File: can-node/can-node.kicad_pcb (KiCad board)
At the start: 4 copper layers, 85 parts, among them J2 Conn_01x04_Pin, J3 USART1, Q1 DMP510DL-7, SW1 KMR2, U1 AP7375-33FDC, U2 STM32F105RBTx, U3 TCAN3404-Q1

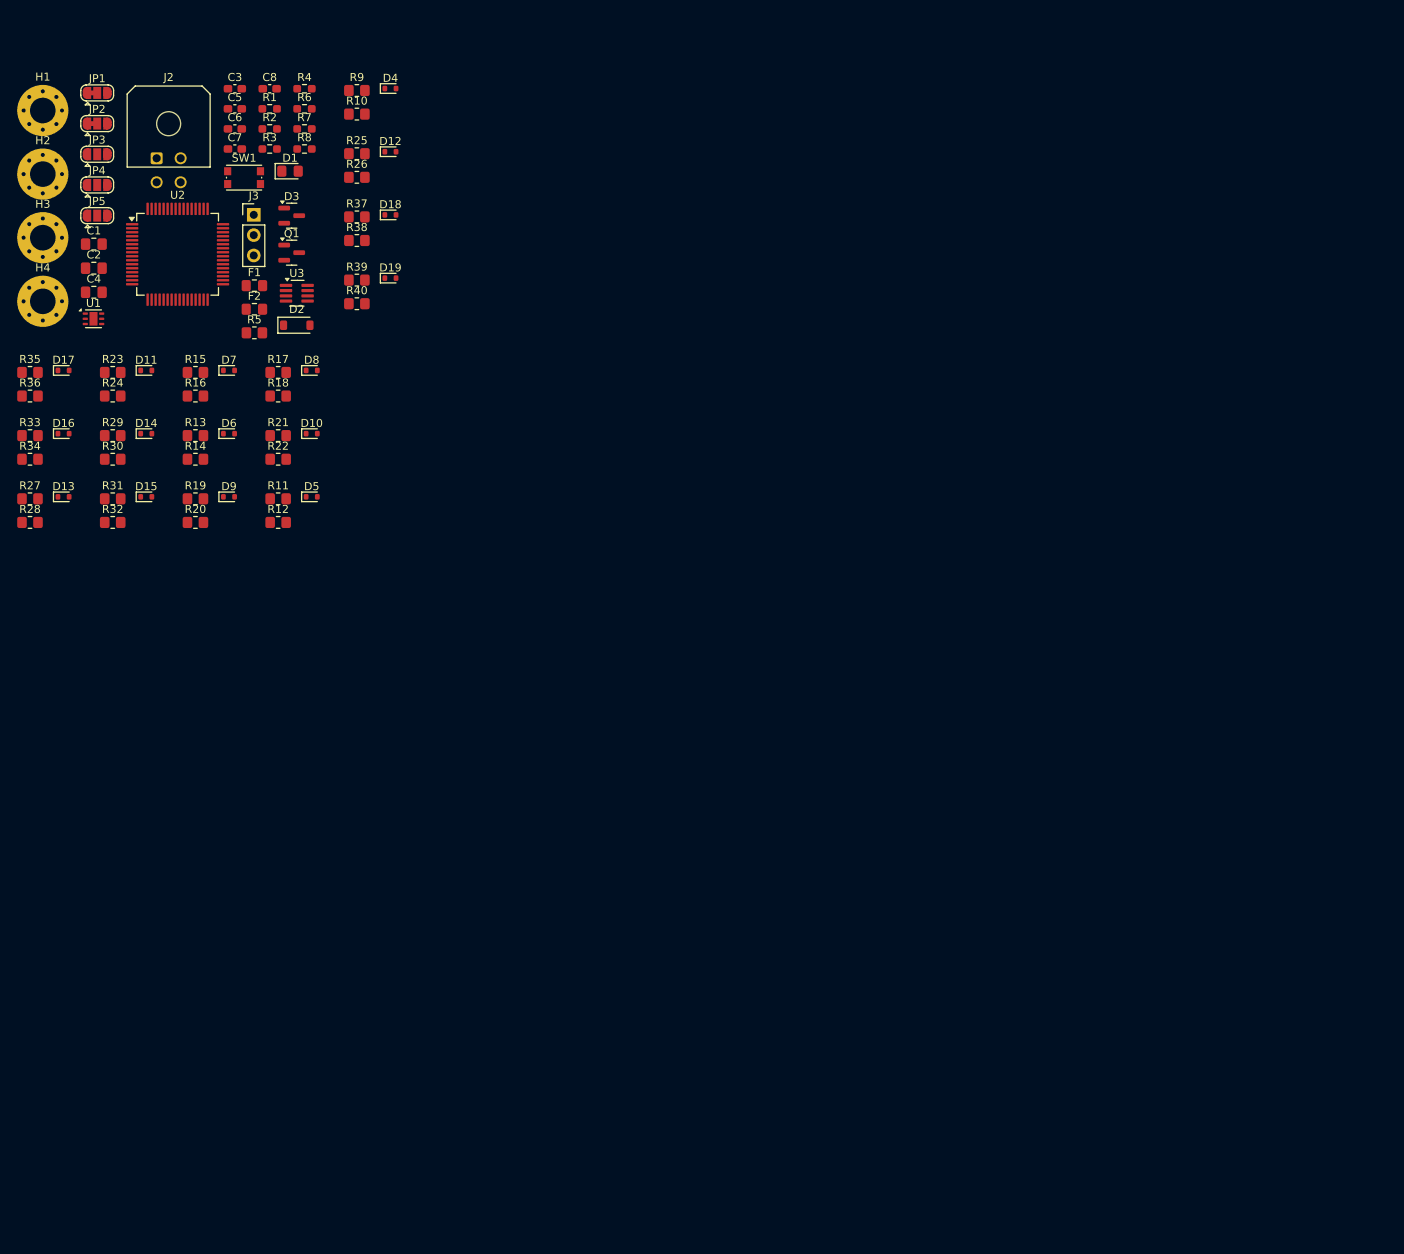
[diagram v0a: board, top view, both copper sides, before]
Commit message: finish routing (not silkscreen)
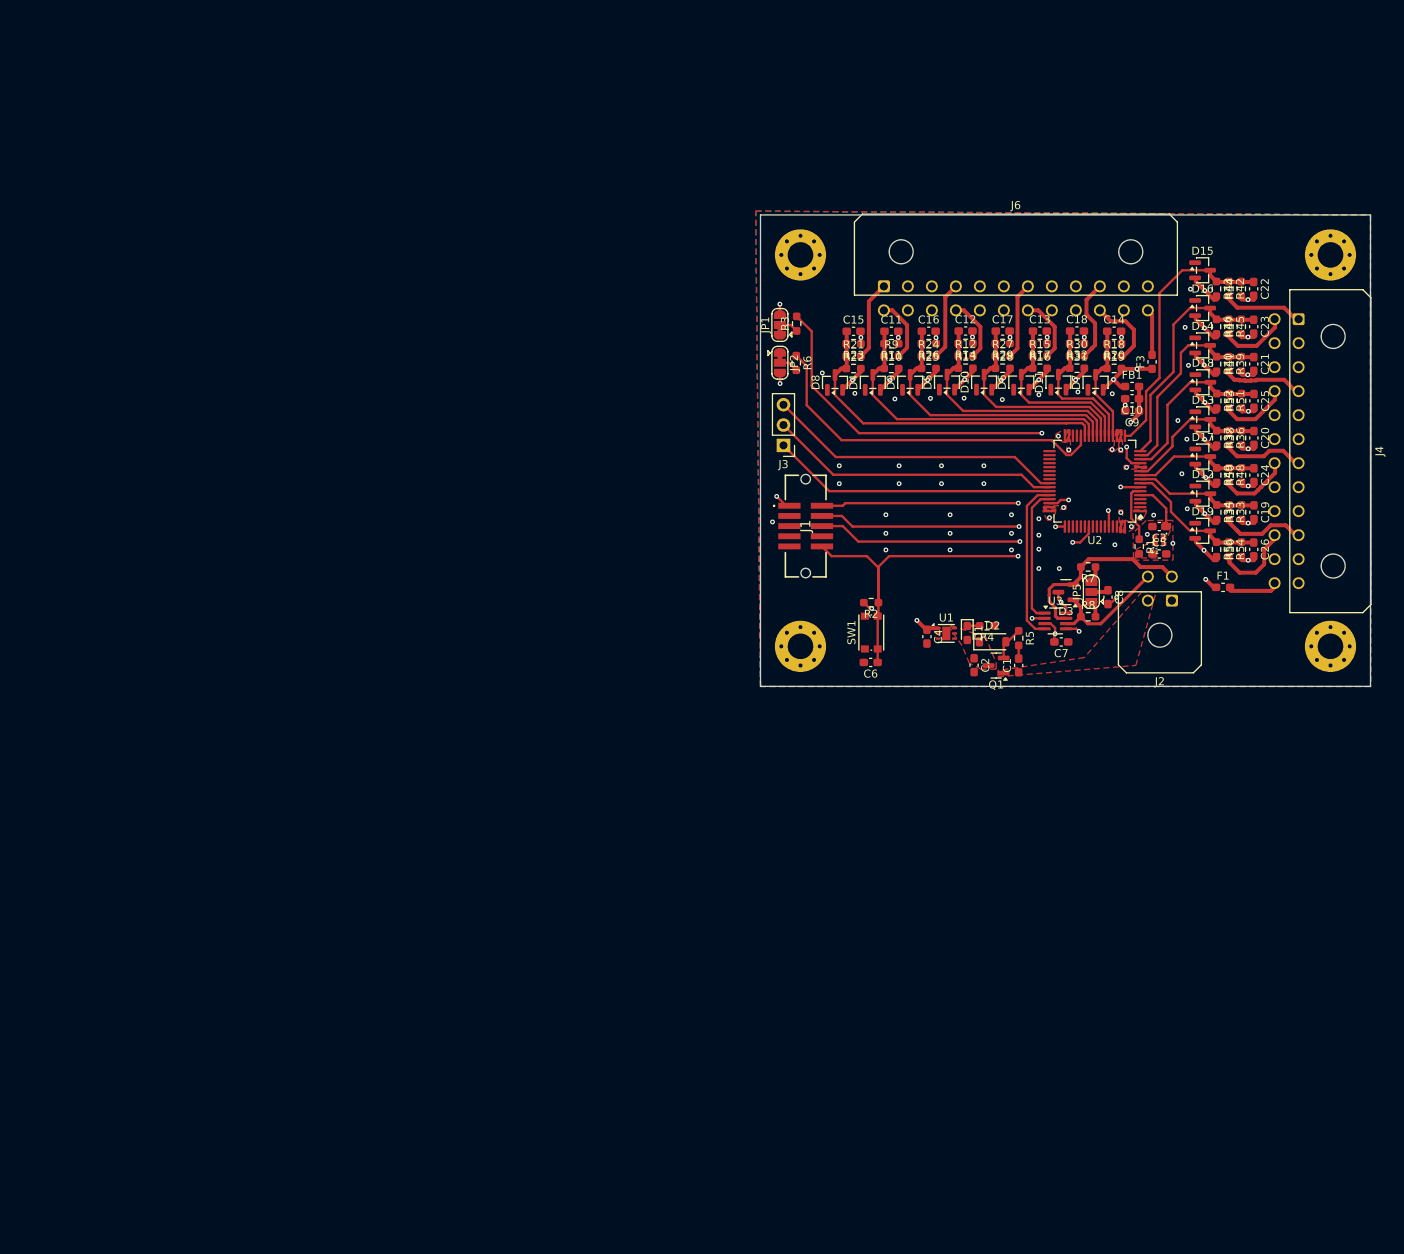
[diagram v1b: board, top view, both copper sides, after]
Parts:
- removed F2: 100mA, Fuse:Fuse_0805_2012Metric_Pad1.15x1.40mm_HandSolder
- removed JP3, JP4: SolderJumper_3_Open, Jumper:SolderJumper-3_P1.3mm_Open_RoundedPad1.0x1.5mm
- added C10: 10uF, Capacitor_SMD:C_0603_1608Metric_Pad1.08x0.95mm_HandSolder, F.Cu at (163.0, 63.8)
- added C11: 10nF, Capacitor_SMD:C_0603_1608Metric_Pad1.08x0.95mm_HandSolder, F.Cu at (132.9, 55.4)
- added C12: 10nF, Capacitor_SMD:C_0603_1608Metric_Pad1.08x0.95mm_HandSolder, F.Cu at (142.2, 55.3)
- added C13: 10nF, Capacitor_SMD:C_0603_1608Metric_Pad1.08x0.95mm_HandSolder, F.Cu at (151.5, 55.3)
- added C14: 10nF, Capacitor_SMD:C_0603_1608Metric_Pad1.08x0.95mm_HandSolder, F.Cu at (160.8, 55.4)
- added C15: 10nF, Capacitor_SMD:C_0603_1608Metric_Pad1.08x0.95mm_HandSolder, F.Cu at (128.2, 55.4)
- added C16: 10nF, Capacitor_SMD:C_0603_1608Metric_Pad1.08x0.95mm_HandSolder, F.Cu at (137.6, 55.4)
- added C17: 10nF, Capacitor_SMD:C_0603_1608Metric_Pad1.08x0.95mm_HandSolder, F.Cu at (146.8, 55.3)
- added C18: 10nF, Capacitor_SMD:C_0603_1608Metric_Pad1.08x0.95mm_HandSolder, F.Cu at (156.1, 55.3)
- added C19: 10nF, Capacitor_SMD:C_0603_1608Metric_Pad1.08x0.95mm_HandSolder, F.Cu at (178.2, 78.0)
- added C20: 10nF, Capacitor_SMD:C_0603_1608Metric_Pad1.08x0.95mm_HandSolder, F.Cu at (178.2, 68.7)
- added C21: 10nF, Capacitor_SMD:C_0603_1608Metric_Pad1.08x0.95mm_HandSolder, F.Cu at (178.2, 59.5)
- added C22: 10nF, Capacitor_SMD:C_0603_1608Metric_Pad1.08x0.95mm_HandSolder, F.Cu at (178.2, 50.1)
- added C23: 10nF, Capacitor_SMD:C_0603_1608Metric_Pad1.08x0.95mm_HandSolder, F.Cu at (178.2, 54.8)
- added C24: 10nF, Capacitor_SMD:C_0603_1608Metric_Pad1.08x0.95mm_HandSolder, F.Cu at (178.2, 73.3)
- added C25: 10nF, Capacitor_SMD:C_0603_1608Metric_Pad1.08x0.95mm_HandSolder, F.Cu at (178.2, 64.1)
- added C26: 10nF, Capacitor_SMD:C_0603_1608Metric_Pad1.08x0.95mm_HandSolder, F.Cu at (178.2, 82.6)
- added C9: 1uF, Capacitor_SMD:C_0603_1608Metric_Pad1.08x0.95mm_HandSolder, F.Cu at (163.0, 65.3)
- added F3: 100mA, Fuse:Fuse_0603_1608Metric_Pad1.05x0.95mm_HandSolder, F.Cu at (165.5, 59.2)
- added FB1: BLM18PG121SN1, Inductor_SMD:L_0603_1608Metric_Pad1.05x0.95mm_HandSolder, F.Cu at (163.0, 62.3)
- added J1: Conn_ARM_JTAG_SWD_10, SUFST:SHF10501LDSMLC, F.Cu at (122.2, 79.7)
- added J4: Molex MicroFit 3.0 24 pin (2x12) 43045-2401, Connector_Molex:Molex_Micro-Fit_3.0_43045-2400_2x12_P3.00mm_Horizontal, F.Cu at (183.8, 53.9)
- added J6: Molex MicroFit 3.0 24 pin (2x12) 43045-2401, Connector_Molex:Molex_Micro-Fit_3.0_43045-2400_2x12_P3.00mm_Horizontal, F.Cu at (132.0, 49.8)
- added R41: 10k, Resistor_SMD:R_0603_1608Metric_Pad0.98x0.95mm_HandSolder, F.Cu at (176.7, 59.5)
- added R42: 40k, Resistor_SMD:R_0603_1608Metric_Pad0.98x0.95mm_HandSolder, F.Cu at (175.1, 50.1)
- added R43: NC, Resistor_SMD:R_0603_1608Metric_Pad0.98x0.95mm_HandSolder, F.Cu at (173.5, 50.1)
- added R44: 10k, Resistor_SMD:R_0603_1608Metric_Pad0.98x0.95mm_HandSolder, F.Cu at (176.6, 50.1)
- added R45: 40k, Resistor_SMD:R_0603_1608Metric_Pad0.98x0.95mm_HandSolder, F.Cu at (175.1, 54.8)
- added R46: NC, Resistor_SMD:R_0603_1608Metric_Pad0.98x0.95mm_HandSolder, F.Cu at (173.6, 54.8)
- added R47: 10k, Resistor_SMD:R_0603_1608Metric_Pad0.98x0.95mm_HandSolder, F.Cu at (176.7, 54.8)
- added R48: 40k, Resistor_SMD:R_0603_1608Metric_Pad0.98x0.95mm_HandSolder, F.Cu at (175.1, 73.3)
- added R49: NC, Resistor_SMD:R_0603_1608Metric_Pad0.98x0.95mm_HandSolder, F.Cu at (173.6, 73.3)
- added R50: 10k, Resistor_SMD:R_0603_1608Metric_Pad0.98x0.95mm_HandSolder, F.Cu at (176.7, 73.3)
- added R51: 40k, Resistor_SMD:R_0603_1608Metric_Pad0.98x0.95mm_HandSolder, F.Cu at (175.1, 64.1)
- added R52: NC, Resistor_SMD:R_0603_1608Metric_Pad0.98x0.95mm_HandSolder, F.Cu at (173.6, 64.1)
- added R53: 10k, Resistor_SMD:R_0603_1608Metric_Pad0.98x0.95mm_HandSolder, F.Cu at (176.7, 64.1)
- added R54: 40k, Resistor_SMD:R_0603_1608Metric_Pad0.98x0.95mm_HandSolder, F.Cu at (175.1, 82.6)
- added R55: NC, Resistor_SMD:R_0603_1608Metric_Pad0.98x0.95mm_HandSolder, F.Cu at (173.6, 82.6)
- added R56: 10k, Resistor_SMD:R_0603_1608Metric_Pad0.98x0.95mm_HandSolder, F.Cu at (176.7, 82.6)
- added Y1: ECS-250-10-47Q-CES-TR, SUFST:Resonator_SMD_ECS_ECX-1247Q_1.6x1.2x0.3mm, F.Cu at (166.4, 81.5)
- C1, C2, C4: footprint Capacitor_SMD:C_0805_2012Metric_Pad1.18x1.45mm_HandSolder -> Capacitor_SMD:C_0603_1608Metric_Pad1.08x0.95mm_HandSolder
- D1: footprint LED_SMD:LED_0805_2012Metric_Pad1.15x1.40mm_HandSolder -> LED_SMD:LED_0603_1608Metric_Pad1.05x0.95mm_HandSolder
- D10, D11, D12, D13, D14, D15, D16, D17, D18, D19, D4, D5, D6, D7, D8, D9: value BZT585B3V3T-7 -> BAT54S; footprint Diode_SMD:D_SOD-523 -> Package_TO_SOT_SMD:SOT-23
- F1: footprint Fuse:Fuse_0805_2012Metric_Pad1.15x1.40mm_HandSolder -> Fuse:Fuse_0603_1608Metric_Pad1.05x0.95mm_HandSolder
- R10, R16, R22, R28, R34, R40: value 40k -> NC; footprint Resistor_SMD:R_0805_2012Metric_Pad1.20x1.40mm_HandSolder -> Resistor_SMD:R_0603_1608Metric_Pad0.98x0.95mm_HandSolder
- R11, R12, R17, R18, R23, R24, R29, R30, R35, R36, R5: footprint Resistor_SMD:R_0805_2012Metric_Pad1.20x1.40mm_HandSolder -> Resistor_SMD:R_0603_1608Metric_Pad0.98x0.95mm_HandSolder
- R13, R19, R25, R31, R37: value 10k -> NC; footprint Resistor_SMD:R_0805_2012Metric_Pad1.20x1.40mm_HandSolder -> Resistor_SMD:R_0603_1608Metric_Pad0.98x0.95mm_HandSolder
- R14, R20, R26, R32, R38: value 40k -> 10k; footprint Resistor_SMD:R_0805_2012Metric_Pad1.20x1.40mm_HandSolder -> Resistor_SMD:R_0603_1608Metric_Pad0.98x0.95mm_HandSolder
- R15, R21, R27, R33, R39, R9: value 10k -> 40k; footprint Resistor_SMD:R_0805_2012Metric_Pad1.20x1.40mm_HandSolder -> Resistor_SMD:R_0603_1608Metric_Pad0.98x0.95mm_HandSolder
- moved H4 166.6 mm to (187.8, 94.8)
- moved H2 161.3 mm to (187.8, 45.8)
- moved R35 152.4 mm to (176.7, 78.0), turned to 90 degrees
- moved R33 150.2 mm to (175.1, 78.0), turned to -90 degrees
- moved R36 150.0 mm to (175.1, 68.7), turned to -90 degrees
- moved R34 148.5 mm to (173.6, 78.0), turned to -90 degrees
- moved D16 143.2 mm to (171.8, 52.5)
- moved D17 142.8 mm to (171.8, 71.0)
- moved D13 142.7 mm to (171.8, 66.4)
- moved J2 138.4 mm to (168.0, 89.0), turned to 180 degrees
- moved D15 135.0 mm to (171.8, 47.7)
- moved JP5 132.9 mm to (157.9, 88.0), turned to 90 degrees
- moved D14 132.5 mm to (171.8, 57.1)
- moved C5 128.3 mm to (166.4, 83.2)
- moved C3 127.9 mm to (166.4, 79.8), turned to 180 degrees
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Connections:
- C4 pad 1: +3.3V -> +3V3
- C7 pad 2: +3.3V -> +3V3
- D10 pad 1: /ADC_1_2 -> GND
- D10 pad 2: GND -> +3V3
- D11 pad 1: /ADC_1_1 -> GND
- D11 pad 2: GND -> +3V3
- D12 pad 1: /ADC_1_0 -> GND
- D12 pad 2: GND -> +3V3
- D13 pad 1: /ADC_0_7 -> GND
- D13 pad 2: GND -> +3V3
- D14 pad 1: /ADC_0_6 -> GND
- D14 pad 2: GND -> +3V3
- D15 pad 1: /ADC_0_5 -> GND
- D15 pad 2: GND -> +3V3
- D16 pad 1: /ADC_0_4 -> GND
- D16 pad 2: GND -> +3V3
- D17 pad 1: /ADC_0_1 -> GND
- D17 pad 2: GND -> +3V3
- D18 pad 1: /ADC_0_3 -> GND
- D18 pad 2: GND -> +3V3
- D19 pad 1: /ADC_0_2 -> GND
- D19 pad 2: GND -> +3V3
- D4 pad 1: /ADC_1_7 -> GND
- D4 pad 2: GND -> +3V3
- D5 pad 1: /ADC_0_0 -> GND
- D5 pad 2: GND -> +3V3
- D6 pad 1: /ADC_1_6 -> GND
- D6 pad 2: GND -> +3V3
- D7 pad 1: /ADC_1_5 -> GND
- D7 pad 2: GND -> +3V3
- D8 pad 1: /ADC_1_4 -> GND
- D8 pad 2: GND -> +3V3
- D9 pad 1: /ADC_1_3 -> GND
- D9 pad 2: GND -> +3V3
- F1 pad 1: GND -> +3V3
- F1 pad 2: Net-(JP3-A) -> /Generic ADC Input Group1/3V3_FUSED
- JP1 pad 3: +3.3V -> +3V3
- R10 pad 1: /ADC_1_7 -> /ADC_0_4
- R10 pad 2: /ClampedDivider15/IN -> +3V3
- R11 pad 2: /ADC_0_0 -> /ADC_0_4
- R12 pad 1: /ADC_0_0 -> /ADC_0_5
- R12 pad 2: /ClampedDivider16/IN -> /Generic ADC Input Group/ClampedDivider17/IN
- R13 pad 1: GND -> /ADC_0_5
- R13 pad 2: /ADC_1_6 -> +3V3
- R14 pad 1: /ADC_1_6 -> GND
- R14 pad 2: /ClampedDivider17/IN -> /ADC_0_5
- R15 pad 1: GND -> /ADC_0_6
- R15 pad 2: /ADC_1_5 -> /Generic ADC Input Group/ClampedDivider18/IN
- R16 pad 1: /ADC_1_5 -> /ADC_0_6
- R16 pad 2: /ClampedDivider18/IN -> +3V3
- R17 pad 2: /ADC_1_4 -> /ADC_0_6
- R18 pad 1: /ADC_1_4 -> /ADC_0_7
- R18 pad 2: /ClampedDivider19/IN -> /Generic ADC Input Group/ClampedDivider19/IN
- R19 pad 1: GND -> /ADC_0_7
- R19 pad 2: /ADC_1_3 -> +3V3
- R20 pad 1: /ADC_1_3 -> GND
- R20 pad 2: /ClampedDivider20/IN -> /ADC_0_7
- R21 pad 1: GND -> /ADC_0_0
- R21 pad 2: /ADC_1_2 -> /Generic ADC Input Group/ClampedDivider20/IN
- R22 pad 1: /ADC_1_2 -> /ADC_0_0
- R22 pad 2: /ClampedDivider21/IN -> +3V3
- R23 pad 2: /ADC_1_1 -> /ADC_0_0
- R24 pad 1: /ADC_1_1 -> /ADC_0_1
- R24 pad 2: /ClampedDivider22/IN -> /Generic ADC Input Group/ClampedDivider21/IN
- R25 pad 1: GND -> /ADC_0_1
- R25 pad 2: /ADC_1_0 -> +3V3
- R26 pad 1: /ADC_1_0 -> GND
- R26 pad 2: /ClampedDivider23/IN -> /ADC_0_1
- R27 pad 1: GND -> /ADC_0_2
- R27 pad 2: /ADC_0_7 -> /Generic ADC Input Group/ClampedDivider22/IN
- R28 pad 1: /ADC_0_7 -> /ADC_0_2
- R28 pad 2: /ClampedDivider24/IN -> +3V3
- R29 pad 2: /ADC_0_6 -> /ADC_0_2
- R30 pad 1: /ADC_0_6 -> /ADC_0_3
- R30 pad 2: /ClampedDivider25/IN -> /Generic ADC Input Group/ClampedDivider23/IN
- R31 pad 1: GND -> /ADC_0_3
- R31 pad 2: /ADC_0_5 -> +3V3
- R32 pad 1: /ADC_0_5 -> GND
- R32 pad 2: /ClampedDivider26/IN -> /ADC_0_3
- R33 pad 1: GND -> /ADC_1_3
- R33 pad 2: /ADC_0_4 -> /Generic ADC Input Group1/ClampedDivider23/IN
- R34 pad 1: /ADC_0_4 -> /ADC_1_3
- R34 pad 2: /ClampedDivider27/IN -> +3V3
- R35 pad 2: /ADC_0_1 -> /ADC_1_3
- R36 pad 1: /ADC_0_1 -> /ADC_1_2
- R36 pad 2: /ClampedDivider28/IN -> /Generic ADC Input Group1/ClampedDivider22/IN
- R37 pad 1: GND -> /ADC_1_2
- R37 pad 2: /ADC_0_3 -> +3V3
- R38 pad 1: /ADC_0_3 -> GND
- R38 pad 2: /ClampedDivider29/IN -> /ADC_1_2
- R39 pad 1: GND -> /ADC_1_1
- R39 pad 2: /ADC_0_2 -> /Generic ADC Input Group1/ClampedDivider21/IN
- R40 pad 1: /ADC_0_2 -> /ADC_1_1
- R40 pad 2: /ClampedDivider30/IN -> +3V3
- R9 pad 1: GND -> /ADC_0_4
- R9 pad 2: /ADC_1_7 -> /Generic ADC Input Group/ClampedDivider16/IN
- U1 pad 1: +3.3V -> +3V3
- U2 pad 1: +3.3V -> +3V3
- U2 pad 10: /ADC_0_2 -> /ADC_1_6
- U2 pad 11: /ADC_0_3 -> /ADC_1_2
- U2 pad 13: +3.3V -> +3V3A
- U2 pad 14: /ADC_0_4 -> /ADC_1_5
- U2 pad 15: /ADC_0_5 -> /ADC_1_1
- U2 pad 16: /ADC_0_6 -> /ADC_1_4
- U2 pad 17: /ADC_0_7 -> /ADC_1_0
- U2 pad 19: +3.3V -> +3V3
- U2 pad 20: /ADC_1_7 -> /ADC_0_7
- U2 pad 21: /ADC_1_6 -> /ADC_0_3
- U2 pad 22: /ADC_1_5 -> /ADC_0_6
- U2 pad 23: /ADC_1_4 -> /ADC_0_2
- U2 pad 24: /ADC_1_3 -> /ADC_0_5
- U2 pad 25: /ADC_1_2 -> /ADC_0_1
- U2 pad 26: /ADC_1_1 -> /ADC_0_4
- U2 pad 27: /ADC_1_0 -> /ADC_0_0
- U2 pad 32: +3.3V -> +3V3
- U2 pad 48: +3.3V -> +3V3
- U2 pad 64: +3.3V -> +3V3
- U2 pad 8: /ADC_0_0 -> /ADC_1_7
- U2 pad 9: /ADC_0_1 -> /ADC_1_3
- U3 pad 3: +3.3V -> +3V3
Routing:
- net +3V3: track 0.00 -> 77.9 mm, vias 0 -> 29
- net /NReset: track 0.00 -> 63.1 mm, vias 0 -> 2
- net Net-(U2-BOOT0): track 0.00 -> 55.8 mm, vias 0 -> 2
- net Net-(U2-PB2): track 0.00 -> 45.3 mm
- net GND: track 0.00 -> 43.4 mm, vias 0 -> 69
- net /ADC_0_0: track 0.00 -> 43.0 mm
- net /ADC_0_4: track 0.00 -> 38.9 mm
- net USART1_CK: track 0.00 -> 37.3 mm
- net USART1_TX: track 0.00 -> 36.5 mm
- net USART1_RX: track 0.00 -> 35.6 mm
- net SYS_JTDO: track 0.00 -> 35.5 mm, vias 0 -> 2
- net /ADC_0_1: track 0.00 -> 34.9 mm
- net /ADC_1_0: track 0.00 -> 33.9 mm
- net SYS_JTMS-SWDIO: track 0.00 -> 33.7 mm, vias 0 -> 2
- net SYS_JTCK-SW: track 0.00 -> 31.0 mm, vias 0 -> 2
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- added copper zone on F.Cu, net +3V3
- added copper zone on In2.Cu, net +3V3
- added copper zone on F.Cu, net +GLV
- added copper zone on F.Cu, net +GLV_PROT
- added copper zone on In1.Cu, net /Generic ADC Input Group/3V3_FUSED
- added copper zone on In1.Cu, net /Generic ADC Input Group1/3V3_FUSED
- added copper zone on B.Cu, net GND
- added copper zone on F.Cu, net GND
- added copper zone on F.Cu, net Net-(C5-Pad1)
- added copper zone on F.Cu, net Net-(U2-PD0)
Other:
- board outline added: 76.3 x 58.9 mm

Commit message: switch B.Cu and In1.Cu routing, update silkscreen and other fixes
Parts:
- added G***: LOGO, SUFST:SUFST, F.Cu at (139.7, 76.1)
- moved R1 9.44 mm to (168.1, 73.8), turned to 0 degrees
- moved C5 7.18 mm to (169.2, 76.6), turned to -90 degrees
- moved Y1 5.30 mm to (166.6, 76.2), turned to 0 degrees
- moved C3 1.94 mm to (166.8, 77.9), turned to 0 degrees
- moved U1 1.52 mm to (139.8, 94.7)
- moved C4 1.52 mm to (137.4, 95.0)
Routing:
- net Net-(U2-BOOT0): track 55.8 -> 63.9 mm
- net /ADC_1_7: track 18.3 -> 24.3 mm
- net Net-(C5-Pad1): track 0.00 -> 4.59 mm
- net GND: track 43.4 -> 47.0 mm, vias 69 -> 98
- net Net-(U2-PD1): track 7.40 -> 4.09 mm
- net Net-(U2-PD0): track 6.18 -> 3.47 mm
- net SYS_JTCK-SW: track 31.0 -> 29.9 mm
- net /ADC_1_3: track 15.9 -> 16.8 mm
- net +3V3: track 77.9 -> 77.1 mm, vias 29 -> 38
- net Net-(D2-A+): track 4.30 -> 3.68 mm
- added copper zone on B.Cu, net /Generic ADC Input Group/3V3_FUSED
- added copper zone on B.Cu, net /Generic ADC Input Group1/3V3_FUSED
- added copper zone on In1.Cu, net GND
- added copper zone on In2.Cu, net GND
- removed copper zone on In1.Cu, net /Generic ADC Input Group/3V3_FUSED
- removed copper zone on In1.Cu, net /Generic ADC Input Group1/3V3_FUSED
- removed copper zone on F.Cu, net Net-(C5-Pad1)
- removed copper zone on F.Cu, net Net-(U2-PD0)
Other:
- outline, holes or cut-outs redrawn
- board text added: "${REFERENCE}"
- board text added: "0"
- board text added: "1"
- board text added: "Author: Antmicro"
- board text added: "BAT54S"
- board text added: "BOOT"
- board text added: "CAP"
- board text added: "CK"
- board text added: "DOWN"
- board text added: "Designed by Sam and Martin"
- board text added: "HUB"
- board text added: "JTAG"
- board text added: "License: Apache-2.0"
- board text added: "Molex MicroFit 3.0 24 pin (2x12) 43045-2401"
- board text added: "Molex Microfit 3.0 4-pin (2x2) 43045-0400"
- board text added: "RX"
- board text added: "SERIES"
- board text added: "Sensor"
- board text added: "TX"
- board text added: "UART"
- board text added: "UP"
- board text added: "v1.0"

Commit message: forgot to save
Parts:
- added U10: TLV9101IDBVR, Package_TO_SOT_SMD:SOT-23-5_HandSoldering, F.Cu at (89.6, 26.7)
- added U11: TLV9101IDBVR, Package_TO_SOT_SMD:SOT-23-5_HandSoldering, F.Cu at (105.2, 19.9)
- added U12: TLV9101IDBVR, Package_TO_SOT_SMD:SOT-23-5_HandSoldering, F.Cu at (105.2, 26.7)
- added U13: TLV9101IDBVR, Package_TO_SOT_SMD:SOT-23-5_HandSoldering, F.Cu at (97.4, 33.4)
- added U14: TLV9101IDBVR, Package_TO_SOT_SMD:SOT-23-5_HandSoldering, F.Cu at (105.2, 40.2)
- added U15: TLV9101IDBVR, Package_TO_SOT_SMD:SOT-23-5_HandSoldering, F.Cu at (105.2, 33.4)
- added U16: TLV9101IDBVR, Package_TO_SOT_SMD:SOT-23-5_HandSoldering, F.Cu at (81.8, 26.7)
- added U17: TLV9101IDBVR, Package_TO_SOT_SMD:SOT-23-5_HandSoldering, F.Cu at (81.8, 33.4)
- added U18: TLV9101IDBVR, Package_TO_SOT_SMD:SOT-23-5_HandSoldering, F.Cu at (81.8, 19.9)
- added U19: TLV9101IDBVR, Package_TO_SOT_SMD:SOT-23-5_HandSoldering, F.Cu at (97.4, 19.9)
- added U4: TLV9101IDBVR, Package_TO_SOT_SMD:SOT-23-5_HandSoldering, F.Cu at (89.6, 40.2)
- added U5: TLV9101IDBVR, Package_TO_SOT_SMD:SOT-23-5_HandSoldering, F.Cu at (89.6, 33.4)
- added U6: TLV9101IDBVR, Package_TO_SOT_SMD:SOT-23-5_HandSoldering, F.Cu at (97.4, 26.7)
- added U7: TLV9101IDBVR, Package_TO_SOT_SMD:SOT-23-5_HandSoldering, F.Cu at (97.4, 40.2)
- added U8: TLV9101IDBVR, Package_TO_SOT_SMD:SOT-23-5_HandSoldering, F.Cu at (81.8, 40.2)
- added U9: TLV9101IDBVR, Package_TO_SOT_SMD:SOT-23-5_HandSoldering, F.Cu at (89.6, 19.9)
- J4: value Molex MicroFit 3.0 24 pin (2x12) 43045-2401 -> Harwin M80-5402642; footprint Connector_Molex:Molex_Micro-Fit_3.0_43045-2400_2x12_P3.00mm_Horizontal -> SUFST:M80-5402642
- J5: renamed from J6; value Molex MicroFit 3.0 24 pin (2x12) 43045-2401 -> Harwin M80-5402642; footprint Connector_Molex:Molex_Micro-Fit_3.0_43045-2400_2x12_P3.00mm_Horizontal -> SUFST:M80-5402642
- moved C19 98.6 mm to (79.7, 75.9), turned to 0 degrees
- moved R35 97.2 mm to (79.7, 83.5), turned to 0 degrees
- moved R33 95.5 mm to (79.7, 78.5), turned to 0 degrees
- moved R34 93.9 mm to (79.7, 81.0), turned to 0 degrees
- moved R41 89.0 mm to (90.9, 83.5), turned to 0 degrees
- moved C21 88.8 mm to (90.9, 75.9), turned to 0 degrees
- moved D12 87.5 mm to (84.3, 77.1)
- moved C20 87.4 mm to (90.9, 63.9), turned to 0 degrees
- moved R39 86.3 mm to (90.9, 78.5), turned to 0 degrees
- moved R38 85.8 mm to (90.9, 71.4), turned to 0 degrees
- moved R40 85.4 mm to (90.9, 81.0), turned to 0 degrees
- moved R36 84.2 mm to (90.9, 66.4), turned to 0 degrees
- moved R37 82.6 mm to (90.9, 68.9), turned to 0 degrees
- moved R44 77.4 mm to (102.2, 71.4), turned to 0 degrees
- moved C22 77.2 mm to (102.2, 63.9), turned to 0 degrees
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- renumbered C3 to C1, C4 to C10, C5 to C2, C6 to C3, C7 to C4, C8 to C5, C9 to C6, C10 to C7, C1 to C8, C2 to C9, D3 to D1, D1 to D3, F3 to F2, JP5 to JP2, JP2 to JP3, R7 to R4, R8 to R5, R5 to R7, R4 to R8, U3 to U1, U1 to U3
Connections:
- C15 pad 1: /ADC_0_0 -> /ADC_1_3
- C16 pad 1: /ADC_0_1 -> /ADC_1_2
- C17 pad 1: /ADC_0_2 -> /ADC_1_1
- C18 pad 1: /ADC_0_3 -> /ADC_1_0
- C19 pad 1: /ADC_1_3 -> /ADC_0_0
- C20 pad 1: /ADC_1_2 -> /ADC_0_1
- C21 pad 1: /ADC_1_1 -> /ADC_0_2
- C22 pad 1: /ADC_1_0 -> /ADC_0_3
- D10 pad 3: /ADC_0_2 -> /ADC_1_1
- D11 pad 3: /ADC_0_3 -> /ADC_1_0
- D12 pad 3: /ADC_1_3 -> /ADC_0_0
- D13 pad 3: /ADC_1_2 -> /ADC_0_1
- D14 pad 3: /ADC_1_1 -> /ADC_0_2
- D15 pad 3: /ADC_1_0 -> /ADC_0_3
- D8 pad 3: /ADC_0_0 -> /ADC_1_3
- D9 pad 3: /ADC_0_1 -> /ADC_1_2
- J4 pad 1: /Generic ADC Input Group1/ClampedDivider20/IN -> unconnected-(J4-Pin_1-Pad1)
- J4 pad 10: /Generic ADC Input Group1/ClampedDivider23/IN -> /Generic ADC Input Group1/3V3_FUSED
- J4 pad 11: GND -> /Generic ADC Input Group1/ClampedDivider23/IN
- J4 pad 12: /Generic ADC Input Group1/3V3_FUSED -> GND
- J4 pad 13: /Generic ADC Input Group1/ClampedDivider16/IN -> /Generic ADC Input Group1/3V3_FUSED
- J4 pad 14: GND -> unconnected-(J4-Pin_14-Pad14)
- J4 pad 15: /Generic ADC Input Group1/3V3_FUSED -> /Generic ADC Input Group1/ClampedDivider16/IN
- J4 pad 16: /Generic ADC Input Group1/ClampedDivider17/IN -> GND
- J4 pad 17: GND -> /Generic ADC Input Group1/3V3_FUSED
- J4 pad 18: /Generic ADC Input Group1/3V3_FUSED -> /Generic ADC Input Group1/ClampedDivider17/IN
- J4 pad 19: /Generic ADC Input Group1/ClampedDivider18/IN -> GND
- J4 pad 2: GND -> /Generic ADC Input Group1/ClampedDivider20/IN
- J4 pad 20: GND -> /Generic ADC Input Group1/3V3_FUSED
- J4 pad 21: /Generic ADC Input Group1/3V3_FUSED -> /Generic ADC Input Group1/ClampedDivider18/IN
- J4 pad 22: /Generic ADC Input Group1/ClampedDivider19/IN -> GND
- J4 pad 23: GND -> /Generic ADC Input Group1/3V3_FUSED
- J4 pad 24: /Generic ADC Input Group1/3V3_FUSED -> /Generic ADC Input Group1/ClampedDivider19/IN
- J4 pad 3: /Generic ADC Input Group1/3V3_FUSED -> GND
- J4 pad 4: /Generic ADC Input Group1/ClampedDivider21/IN -> /Generic ADC Input Group1/3V3_FUSED
- J4 pad 5: GND -> /Generic ADC Input Group1/ClampedDivider21/IN
- J4 pad 6: /Generic ADC Input Group1/3V3_FUSED -> GND
- J4 pad 7: /Generic ADC Input Group1/ClampedDivider22/IN -> /Generic ADC Input Group1/3V3_FUSED
- J4 pad 8: GND -> /Generic ADC Input Group1/ClampedDivider22/IN
- J4 pad 9: /Generic ADC Input Group1/3V3_FUSED -> GND
- J5 pad 1: /Generic ADC Input Group/ClampedDivider20/IN -> unconnected-(J5-Pin_1-Pad1)
- J5 pad 10: /Generic ADC Input Group/ClampedDivider23/IN -> /Generic ADC Input Group/3V3_FUSED
- J5 pad 11: GND -> /Generic ADC Input Group/ClampedDivider23/IN
- J5 pad 12: /Generic ADC Input Group/3V3_FUSED -> GND
- J5 pad 13: /Generic ADC Input Group/ClampedDivider16/IN -> /Generic ADC Input Group/3V3_FUSED
- J5 pad 14: GND -> unconnected-(J5-Pin_14-Pad14)
- J5 pad 15: /Generic ADC Input Group/3V3_FUSED -> /Generic ADC Input Group/ClampedDivider16/IN
- J5 pad 16: /Generic ADC Input Group/ClampedDivider17/IN -> GND
- J5 pad 17: GND -> /Generic ADC Input Group/3V3_FUSED
- J5 pad 18: /Generic ADC Input Group/3V3_FUSED -> /Generic ADC Input Group/ClampedDivider17/IN
- J5 pad 19: /Generic ADC Input Group/ClampedDivider18/IN -> GND
- J5 pad 2: GND -> /Generic ADC Input Group/ClampedDivider20/IN
- J5 pad 20: GND -> /Generic ADC Input Group/3V3_FUSED
- J5 pad 21: /Generic ADC Input Group/3V3_FUSED -> /Generic ADC Input Group/ClampedDivider18/IN
- J5 pad 22: /Generic ADC Input Group/ClampedDivider19/IN -> GND
- J5 pad 23: GND -> /Generic ADC Input Group/3V3_FUSED
- J5 pad 24: /Generic ADC Input Group/3V3_FUSED -> /Generic ADC Input Group/ClampedDivider19/IN
- J5 pad 3: /Generic ADC Input Group/3V3_FUSED -> GND
- J5 pad 4: /Generic ADC Input Group/ClampedDivider21/IN -> /Generic ADC Input Group/3V3_FUSED
- J5 pad 5: GND -> /Generic ADC Input Group/ClampedDivider21/IN
- J5 pad 6: /Generic ADC Input Group/3V3_FUSED -> GND
- J5 pad 7: /Generic ADC Input Group/ClampedDivider22/IN -> /Generic ADC Input Group/3V3_FUSED
- J5 pad 8: GND -> /Generic ADC Input Group/ClampedDivider22/IN
- J5 pad 9: /Generic ADC Input Group/3V3_FUSED -> GND
- R12 pad 2: /Generic ADC Input Group/ClampedDivider17/IN -> Net-(U5--)
- R15 pad 2: /Generic ADC Input Group/ClampedDivider18/IN -> Net-(U6--)
- R18 pad 2: /Generic ADC Input Group/ClampedDivider19/IN -> Net-(U7--)
- R21 pad 1: /ADC_0_0 -> /ADC_1_3
- R21 pad 2: /Generic ADC Input Group/ClampedDivider20/IN -> Net-(U11--)
- R22 pad 1: /ADC_0_0 -> /ADC_1_3
- R23 pad 2: /ADC_0_0 -> /ADC_1_3
- R24 pad 1: /ADC_0_1 -> /ADC_1_2
- R24 pad 2: /Generic ADC Input Group/ClampedDivider21/IN -> Net-(U10--)
- R25 pad 1: /ADC_0_1 -> /ADC_1_2
- R26 pad 2: /ADC_0_1 -> /ADC_1_2
- R27 pad 1: /ADC_0_2 -> /ADC_1_1
- R27 pad 2: /Generic ADC Input Group/ClampedDivider22/IN -> Net-(U9--)
- R28 pad 1: /ADC_0_2 -> /ADC_1_1
- R29 pad 2: /ADC_0_2 -> /ADC_1_1
- R30 pad 1: /ADC_0_3 -> /ADC_1_0
- R30 pad 2: /Generic ADC Input Group/ClampedDivider23/IN -> Net-(U8--)
- R31 pad 1: /ADC_0_3 -> /ADC_1_0
- R32 pad 2: /ADC_0_3 -> /ADC_1_0
- R33 pad 1: /ADC_1_3 -> /ADC_0_0
- R33 pad 2: /Generic ADC Input Group1/ClampedDivider23/IN -> Net-(U12--)
- R34 pad 1: /ADC_1_3 -> /ADC_0_0
- R35 pad 2: /ADC_1_3 -> /ADC_0_0
- R36 pad 1: /ADC_1_2 -> /ADC_0_1
- R36 pad 2: /Generic ADC Input Group1/ClampedDivider22/IN -> Net-(U13--)
- R37 pad 1: /ADC_1_2 -> /ADC_0_1
- R38 pad 2: /ADC_1_2 -> /ADC_0_1
- R39 pad 1: /ADC_1_1 -> /ADC_0_2
- R39 pad 2: /Generic ADC Input Group1/ClampedDivider21/IN -> Net-(U14--)
- R40 pad 1: /ADC_1_1 -> /ADC_0_2
- R41 pad 2: /ADC_1_1 -> /ADC_0_2
- R42 pad 1: /ADC_1_0 -> /ADC_0_3
- R42 pad 2: /Generic ADC Input Group1/ClampedDivider20/IN -> Net-(U15--)
- R43 pad 1: /ADC_1_0 -> /ADC_0_3
- R44 pad 2: /ADC_1_0 -> /ADC_0_3
- R45 pad 2: /Generic ADC Input Group1/ClampedDivider16/IN -> Net-(U16--)
- R48 pad 2: /Generic ADC Input Group1/ClampedDivider18/IN -> Net-(U17--)
- R51 pad 2: /Generic ADC Input Group1/ClampedDivider17/IN -> Net-(U18--)
- R54 pad 2: /Generic ADC Input Group1/ClampedDivider19/IN -> Net-(U19--)
- R9 pad 2: /Generic ADC Input Group/ClampedDivider16/IN -> Net-(U4--)
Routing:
- net unconnected-(J5-Pin_1-Pad1): track 0.00 -> 11.5 mm
- net /Generic ADC Input Group1/ClampedDivider23/IN: track 10.4 -> 0.00 mm
- net /Generic ADC Input Group/ClampedDivider23/IN: track 10.4 -> 0.00 mm
- net /Generic ADC Input Group1/ClampedDivider22/IN: track 10.2 -> 0.00 mm
- net /Generic ADC Input Group1/ClampedDivider20/IN: track 9.91 -> 0.00 mm
- net /Generic ADC Input Group/ClampedDivider20/IN: track 9.91 -> 0.00 mm
- net /Generic ADC Input Group1/ClampedDivider21/IN: track 9.85 -> 0.00 mm
- net /Generic ADC Input Group/ClampedDivider21/IN: track 9.74 -> 0.00 mm
- net /Generic ADC Input Group/ClampedDivider22/IN: track 9.62 -> 0.00 mm
- net /Generic ADC Input Group1/ClampedDivider19/IN: track 9.35 -> 0.00 mm
- net /Generic ADC Input Group/ClampedDivider19/IN: track 9.35 -> 0.00 mm
- net /Generic ADC Input Group/ClampedDivider18/IN: track 8.23 -> 0.00 mm
- net /Generic ADC Input Group/ClampedDivider17/IN: track 7.93 -> 0.00 mm
- net /Generic ADC Input Group1/ClampedDivider18/IN: track 7.93 -> 0.00 mm
- net /Generic ADC Input Group1/ClampedDivider17/IN: track 7.70 -> 0.00 mm
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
